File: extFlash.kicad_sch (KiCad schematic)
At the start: 3 parts, among them U8 BY25Q32ES

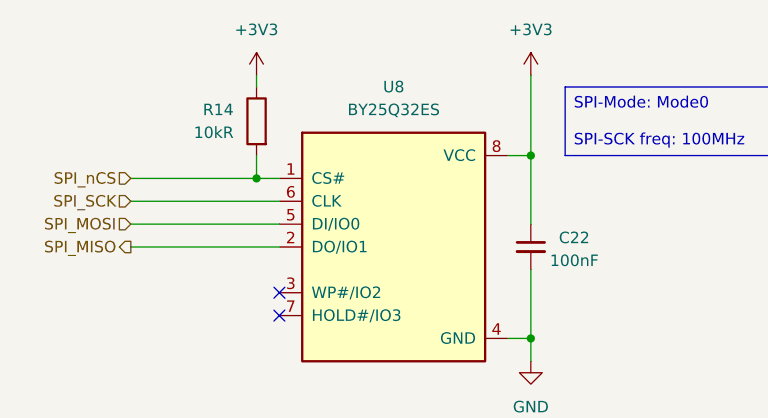
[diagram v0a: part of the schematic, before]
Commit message: Changed LDO to Buc-Boost
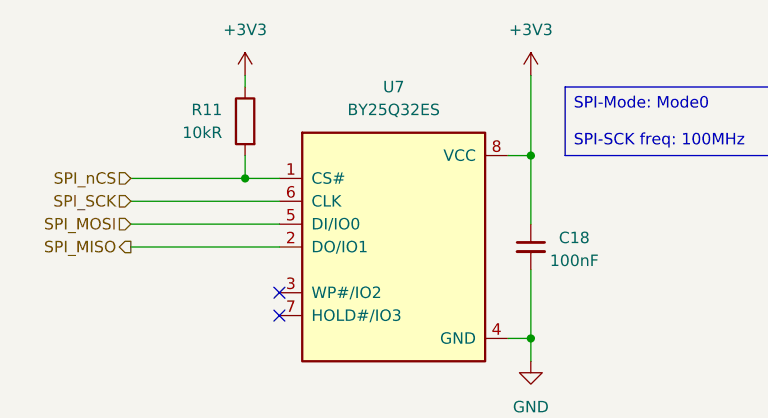
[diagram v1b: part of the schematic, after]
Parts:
- C18: renamed from C22; footprint (none) -> Capacitor_SMD:C_0805_2012Metric_Pad1.18x1.45mm_HandSolder
- R11: renamed from R14; footprint (none) -> Resistor_SMD:R_0805_2012Metric_Pad1.20x1.40mm_HandSolder
- renumbered U8 to U7
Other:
- moved on the sheet: R11
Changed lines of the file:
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@@
 	)
 	(junction
-		(at 57.15 52.07)
+		(at 55.88 52.07)
 		(diameter 0)
 		(color 0 0 0 0)
@@
 	(wire
 		(pts
-			(xy 43.18 52.07) (xy 57.15 52.07)
+			(xy 43.18 52.07) (xy 55.88 52.07)
 		)
 		(stroke
@@
 	(wire
 		(pts
-			(xy 57.15 40.64) (xy 57.15 41.91)
+			(xy 55.88 52.07) (xy 59.69 52.07)
+		)
+		(stroke
+			(width 0)
+			(type default)
+		)
+	)
+	(wire
+		(pts
+			(xy 55.88 40.64) (xy 55.88 41.91)
 		)
 		(stroke
@@
 	(wire
 		(pts
-			(xy 57.15 52.07) (xy 59.69 52.07)
-		)
-		(stroke
-			(width 0)
-			(type default)
-		)
-	)
-	(wire
-		(pts
 			(xy 87.63 72.39) (xy 87.63 69.85)
 		)
@@
 	(wire
 		(pts
-			(xy 57.15 49.53) (xy 57.15 52.07)
+			(xy 55.88 49.53) (xy 55.88 52.07)
 		)
 		(stroke
@@
 		(dnp no)
 		(fields_autoplaced yes)
-		(property "Reference" "#PWR030"
+		(property "Reference" "#PWR027"
 			(at 87.63 78.74 0)
 			(effects
@@
 			(project ""
 				(path "/98695d9f-8521-4f7d-bb41-f22c1215a8e7/54eab4e0-8e74-4f4e-a800-9efd5c437213"
-					(reference "#PWR030")
+					(reference "#PWR027")
 					(unit 1)
 				)
@@
 		(dnp no)
 		(fields_autoplaced yes)
-		(property "Reference" "U8"
+		(property "Reference" "U7"
 			(at 72.39 41.91 0)
 			(effects
@@
 			(project ""
 				(path "/98695d9f-8521-4f7d-bb41-f22c1215a8e7/54eab4e0-8e74-4f4e-a800-9efd5c437213"
-					(reference "U8")
+					(reference "U7")
 					(unit 1)
 				)
@@
 		(dnp no)
 		(fields_autoplaced yes)
-		(property "Reference" "#PWR029"
+		(property "Reference" "#PWR026"
 			(at 87.63 44.45 0)
 			(effects
@@
 			(project ""
 				(path "/98695d9f-8521-4f7d-bb41-f22c1215a8e7/54eab4e0-8e74-4f4e-a800-9efd5c437213"
-					(reference "#PWR029")
+					(reference "#PWR026")
 					(unit 1)
 				)
@@
 		(on_board yes)
 		(dnp no)
-		(property "Reference" "C22"
+		(property "Reference" "C18"
 			(at 92.456 58.674 0)
 			(effects
@@
 			)
 		)
-		(property "Footprint" ""
+		(property "Footprint" "Capacitor_SMD:C_0805_2012Metric_Pad1.18x1.45mm_HandSolder"
 			(at 87.63 59.69 0)
 			(effects
@@
 			(project "Snail_v1"
 				(path "/98695d9f-8521-4f7d-bb41-f22c1215a8e7/54eab4e0-8e74-4f4e-a800-9efd5c437213"
-					(reference "C22")
+					(reference "C18")
 					(unit 1)
 				)
@@
 	(symbol
 		(lib_id "Device:R")
-		(at 57.15 45.72 0)
+		(at 55.88 45.72 0)
 		(mirror y)
 		(unit 1)
@@
 		(on_board yes)
 		(dnp no)
-		(property "Reference" "R14"
-			(at 54.61 44.4499 0)
+		(property "Reference" "R11"
+			(at 53.34 44.4499 0)
 			(effects
 				(font
@@
 		)
 		(property "Value" "10kR"
-			(at 54.61 46.9899 0)
+			(at 53.34 46.9899 0)
 			(effects
 				(font
@@
 			)
 		)
-		(property "Footprint" ""
-			(at 58.928 45.72 90)
+		(property "Footprint" "Resistor_SMD:R_0805_2012Metric_Pad1.20x1.40mm_HandSolder"
+			(at 57.658 45.72 90)
 			(effects
 				(font
@@
 		)
 		(property "Datasheet" "~"
-			(at 57.15 45.72 0)
+			(at 55.88 45.72 0)
 			(effects
 				(font
@@
 		)
 		(property "Description" "Resistor"
-			(at 57.15 45.72 0)
+			(at 55.88 45.72 0)
 			(effects
 				(font
@@
 			(project ""
 				(path "/98695d9f-8521-4f7d-bb41-f22c1215a8e7/54eab4e0-8e74-4f4e-a800-9efd5c437213"
-					(reference "R14")
+					(reference "R11")
 					(unit 1)
 				)
@@
 	(symbol
 		(lib_id "power:+3V3")
-		(at 57.15 40.64 0)
+		(at 55.88 40.64 0)
 		(unit 1)
 		(exclude_from_sim no)
@@
 		(dnp no)
 		(fields_autoplaced yes)
-		(property "Reference" "#PWR031"
-			(at 57.15 44.45 0)
+		(property "Reference" "#PWR025"
+			(at 55.88 44.45 0)
 			(effects
 				(font
@@
 		)
 		(property "Value" "+3V3"
-			(at 57.15 35.56 0)
+			(at 55.88 35.56 0)
 			(effects
 				(font
@@
 		)
 		(property "Footprint" ""
-			(at 57.15 40.64 0)
+			(at 55.88 40.64 0)
 			(effects
 				(font
@@
 		)
 		(property "Datasheet" ""
-			(at 57.15 40.64 0)
+			(at 55.88 40.64 0)
 			(effects
 				(font
@@
 		)
 		(property "Description" "Power symbol creates a global label with name \"+3V3\""
-			(at 57.15 40.64 0)
+			(at 55.88 40.64 0)
 			(effects
 				(font
@@
 			(project "Snail_v1"
 				(path "/98695d9f-8521-4f7d-bb41-f22c1215a8e7/54eab4e0-8e74-4f4e-a800-9efd5c437213"
-					(reference "#PWR031")
+					(reference "#PWR025")
 					(unit 1)
 				)

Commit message: Started with layout
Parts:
- U7: footprint BY25Q32ES.pretty:BY25Q32ES_SOIC-8_150mil -> BY25Q32ES:BY25Q32ESSIG_SOIC-8_208mil
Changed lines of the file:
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@@
 			)
 		)
-		(property "Footprint" "BY25Q32ES.pretty:BY25Q32ES_SOIC-8_150mil"
+		(property "Footprint" "BY25Q32ES:BY25Q32ESSIG_SOIC-8_208mil"
 			(at 74.93 77.724 0)
 			(effects

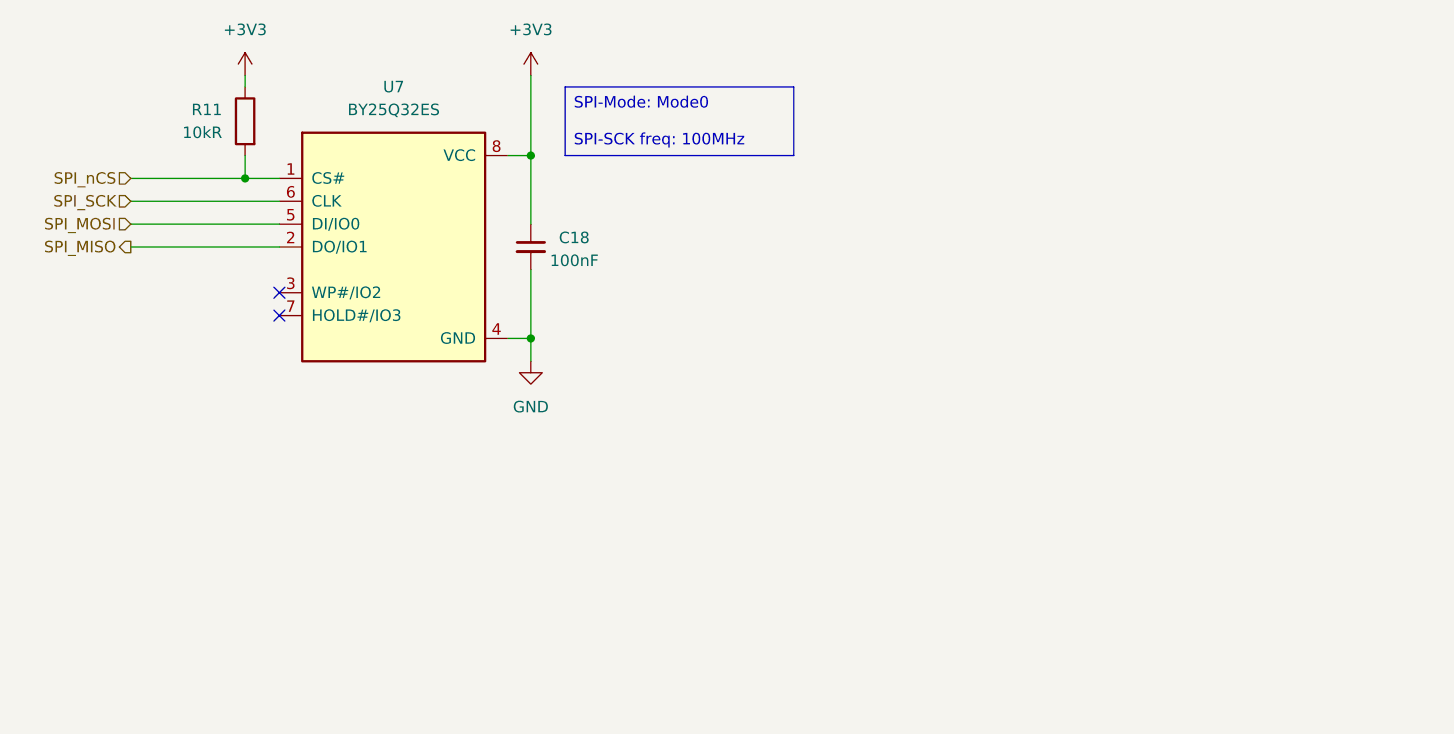
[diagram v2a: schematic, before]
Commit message: Did Silkscreen + added images of PCBA
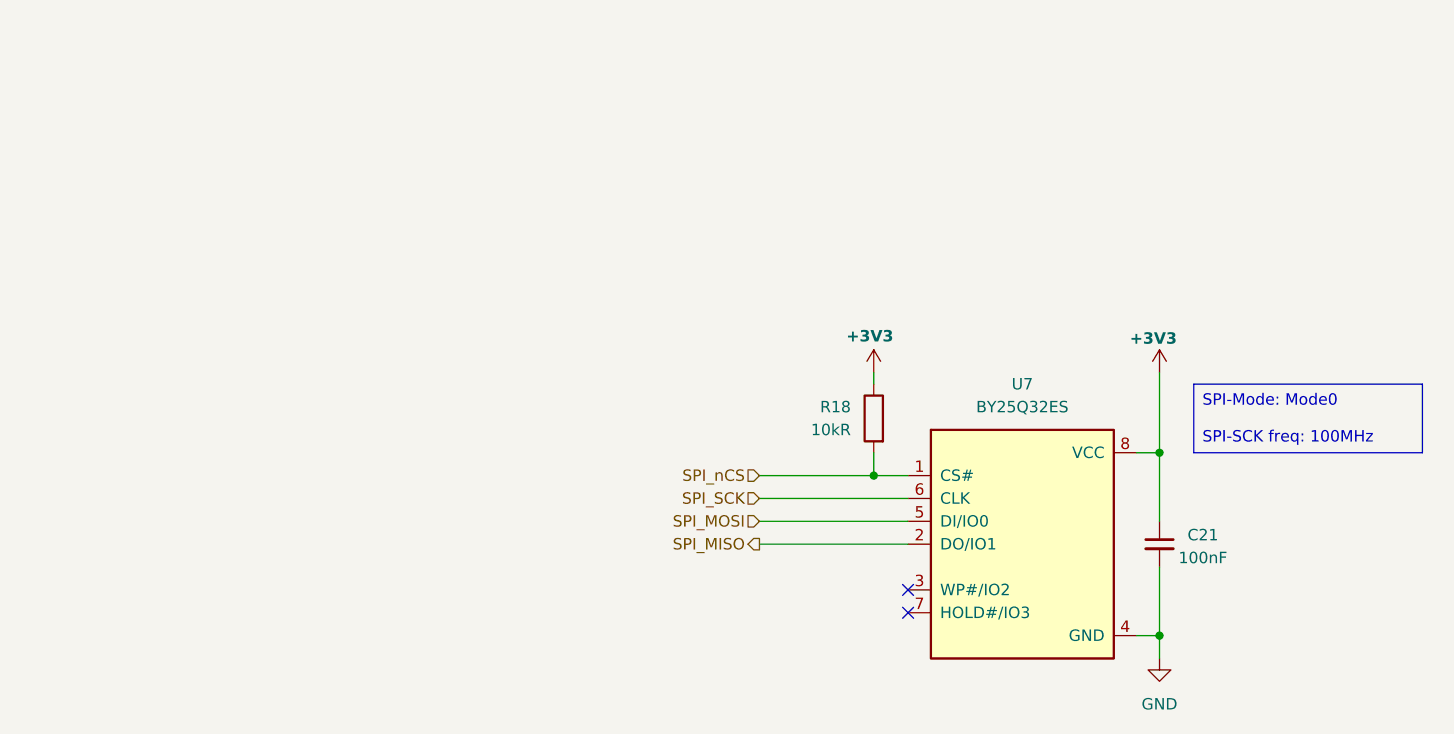
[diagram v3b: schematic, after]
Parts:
- renumbered C18 to C21, R11 to R18
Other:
- moved on the sheet: C21, R18, U7

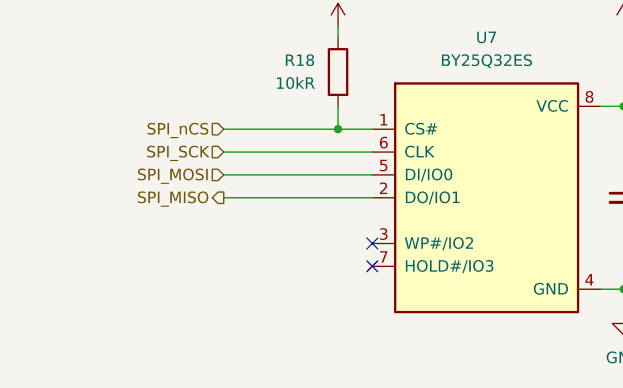
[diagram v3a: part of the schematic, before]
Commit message: Added missing AMP_nSD connection to MCU via 5V_EN
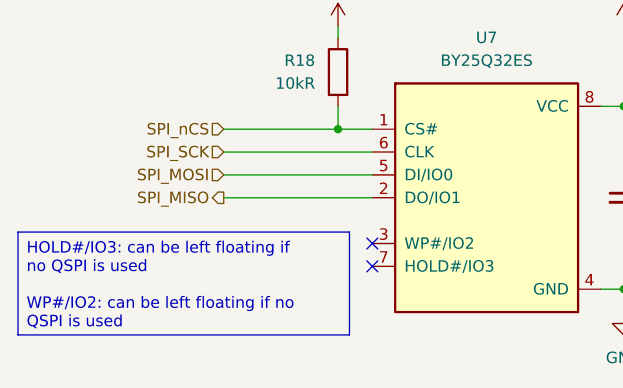
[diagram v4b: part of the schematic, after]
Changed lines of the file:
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@@
+		)
+	)
+	(text_box "HOLD#/IO3: can be left floating if no QSPI is used\n\nWP#/IO2: can be left floating if no QSPI is used"
+		(exclude_from_sim no)
+		(at 90.17 96.52 0)
+		(size 36.83 11.43)
+		(margins 0.9525 0.9525 0.9525 0.9525)
+		(stroke
+			(width 0)
+			(type solid)
+		)
+		(fill
+			(type none)
+		)
+		(effects
+			(font
+				(size 1.27 1.27)
+			)
+			(justify left top)
 		)
 	)
